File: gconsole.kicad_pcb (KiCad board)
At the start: 2 copper layers, 2 parts, among them SW1 SW_Push, U1 XIAO-ESP32-C3-DIP

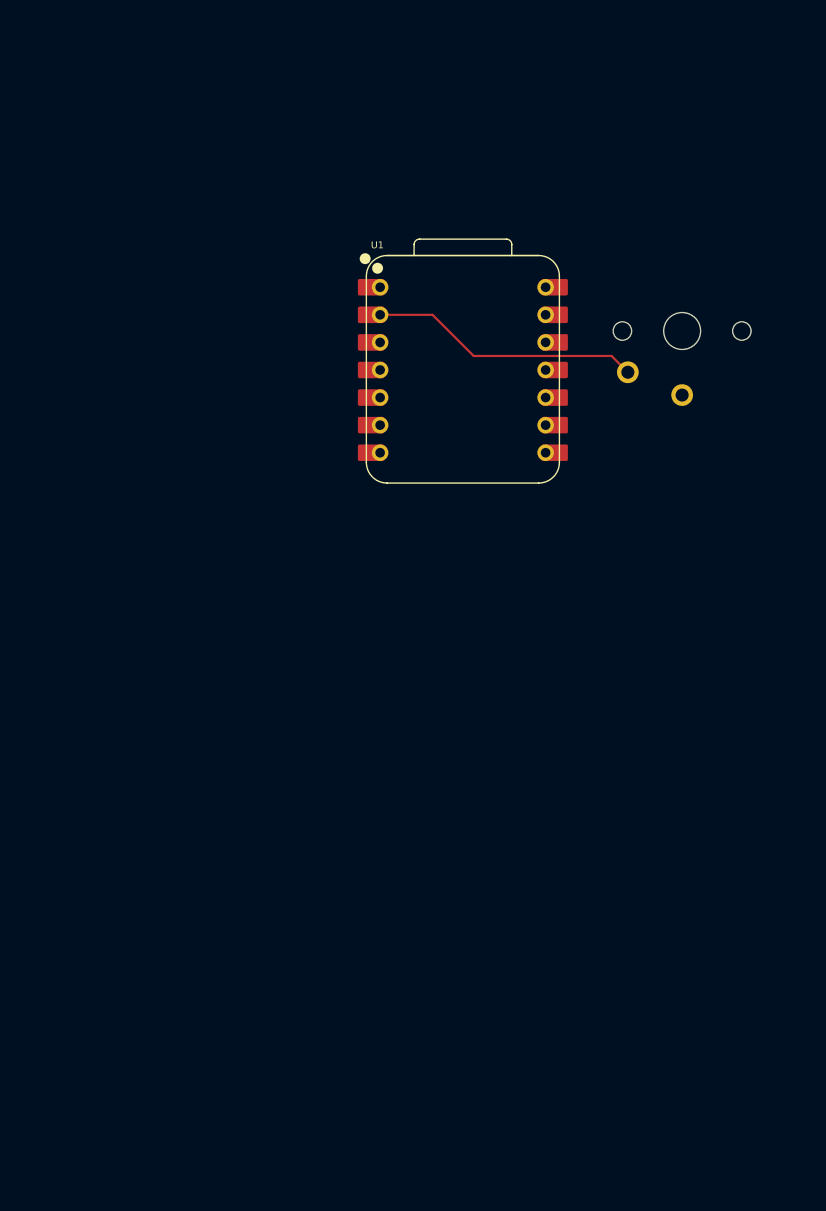
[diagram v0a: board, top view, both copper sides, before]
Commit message: Imported modules in KiCad
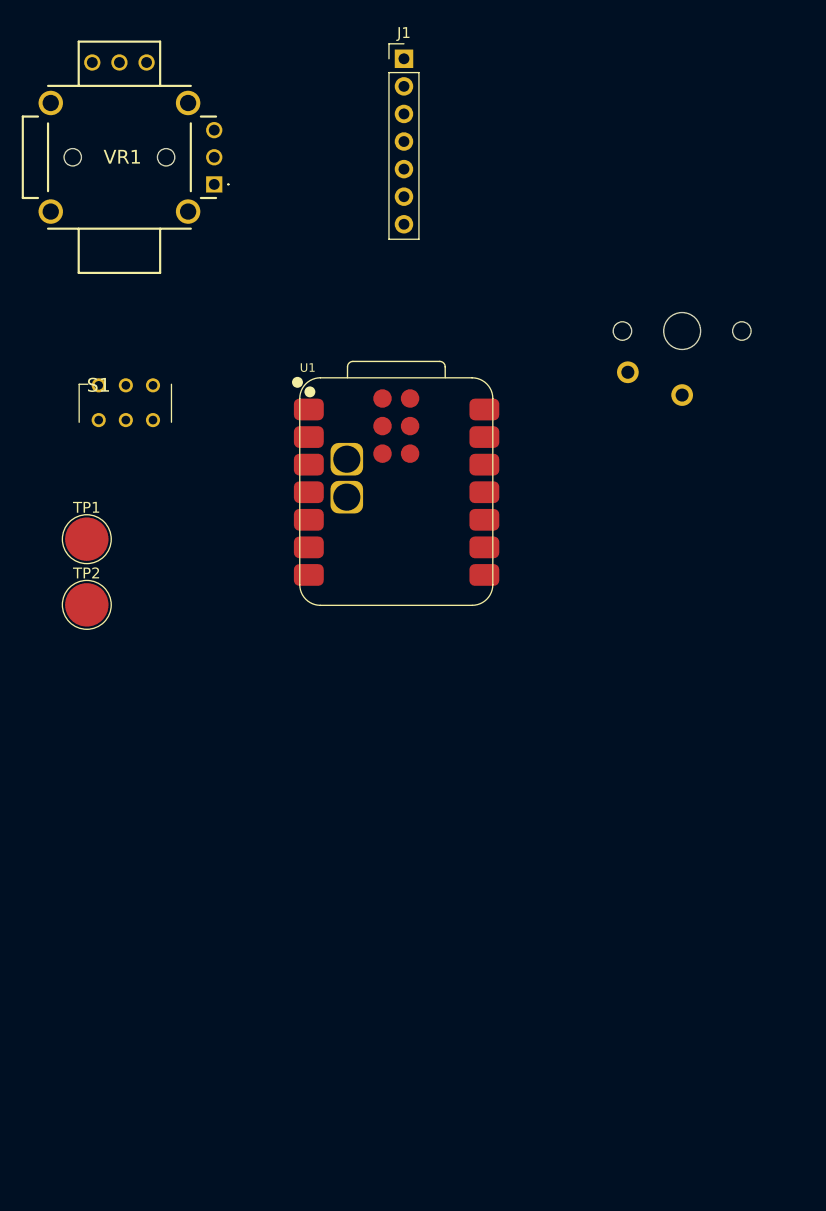
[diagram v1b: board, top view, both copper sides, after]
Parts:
- added J1: Conn_01x07_Socket, Connector_PinHeader_2.54mm:PinHeader_1x07_P2.54mm_Vertical, F.Cu at (119.4, 74.9)
- added S1: EG1271A, KiCad:EG1271, F.Cu at (91.3, 105.0)
- added TP1: TestPoint, TestPoint:TestPoint_Pad_D4.0mm, F.Cu at (90.2, 119.2)
- added TP2: TestPoint, TestPoint:TestPoint_Pad_D4.0mm, F.Cu at (90.2, 125.2)
- added VR1: RKJXV1224005, joystick:RKJXV1224005, F.Cu at (101.9, 86.5)
- U1: footprint Seeed Studio XIAO Series Library:XIAO-ESP32C3-DIP -> Seeed Studio XIAO Series Library:XIAO-ESP32C3-SMD
- moved U1 12.9 mm to (118.6, 114.8)
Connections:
- SW1 pad 1: Net-(U1-GPIO3/A1/D1) -> unconnected-(SW1-Pad1)
- U1 pad 2: Net-(U1-GPIO3/A1/D1) -> unconnected-(U1-GPIO3/A1/D1-Pad2)
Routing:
- net Net-(U1-GPIO3/A1/D1): track 25.0 -> 0.00 mm

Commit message: Finished designing PCB
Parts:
- added H1: MountingHole, MountingHole:MountingHole_3.2mm_M3, F.Cu at (145.5, 93.0)
- added H2: MountingHole, MountingHole:MountingHole_3.2mm_M3, F.Cu at (106.1, 92.9)
- added H3: MountingHole, MountingHole:MountingHole_3.2mm_M3, F.Cu at (106.2, 170.4)
- added H4: MountingHole, MountingHole:MountingHole_3.2mm_M3, F.Cu at (145.5, 170.4)
- S1, TP1, TP2: moved to B.Cu
- U1: value XIAO-ESP32-C3-DIP -> XIAO-ESP32-C3-SMD; footprint Seeed Studio XIAO Series Library:XIAO-ESP32C3-SMD -> Seeed Studio XIAO Series Library:XIAO-ESP32C3-SMD-modified; moved to B.Cu
- moved VR1 73.0 mm to (123.0, 156.4)
- moved SW1 54.1 mm to (136.7, 153.4)
- moved TP1 48.8 mm to (137.7, 130.3), turned to 180 degrees
- moved TP2 48.8 mm to (137.7, 136.4), turned to 180 degrees
- moved S1 38.8 mm to (130.0, 107.0), turned to -90 degrees
- moved J1 25.4 mm to (132.8, 96.5), turned to -90 degrees
- moved U1 4.38 mm to (114.3, 114.3), turned to -90 degrees
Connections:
- J1 pad 1: unconnected-(J1-Pin_1-Pad1) -> Net-(J1-Pin_1)
- J1 pad 2: unconnected-(J1-Pin_2-Pad2) -> Net-(J1-Pin_2)
- J1 pad 3: unconnected-(J1-Pin_3-Pad3) -> Net-(J1-Pin_3)
- J1 pad 4: unconnected-(J1-Pin_4-Pad4) -> Net-(J1-Pin_4)
- J1 pad 5: unconnected-(J1-Pin_5-Pad5) -> Net-(J1-Pin_5)
- J1 pad 6: unconnected-(J1-Pin_6-Pad6) -> +3V3
- J1 pad 7: unconnected-(J1-Pin_7-Pad7) -> GND
- S1 pad 2: unconnected-(S1-COM_1-Pad2) -> /+BAT
- S1 pad 3: unconnected-(S1-NO_1-Pad3) -> Net-(S1-NO_1)
- SW1 pad 1: unconnected-(SW1-Pad1) -> Net-(U1-GPIO20_D7_RX)
- SW1 pad 2: unconnected-(SW1-Pad2) -> GND
- TP1 pad 1: unconnected-(TP1-Pad1) -> GND
- TP2 pad 1: unconnected-(TP2-Pad1) -> /+BAT
- U1 pad 1: unconnected-(U1-GPIO2/A0/D0-Pad1) -> Net-(U1-GPIO2_A0_D0)
- U1 pad 11: unconnected-(U1-GPIO10/D10/MOSI-Pad11) -> Net-(J1-Pin_4)
- U1 pad 12: unconnected-(U1-VCC_3V3-Pad12) -> +3V3
- U1 pad 13: unconnected-(U1-GND-Pad13) -> GND
- U1 pad 15: (no net) -> Net-(S1-NO_1)
- U1 pad 16: (no net) -> GND
- U1 pad 17: (no net) -> unconnected-(U1-MTDI-Pad17)
- U1 pad 18: (no net) -> unconnected-(U1-MTDO-Pad18)
- U1 pad 19: (no net) -> unconnected-(U1-CHIP_EN-Pad19)
- U1 pad 2: unconnected-(U1-GPIO3/A1/D1-Pad2) -> Net-(U1-GPIO3_A1_D1)
- U1 pad 20: (no net) -> GND
- U1 pad 21: (no net) -> unconnected-(U1-MTMS-Pad21)
- U1 pad 22: (no net) -> unconnected-(U1-MTCK-Pad22)
- U1 pad 5: unconnected-(U1-GPIO6/D4/SDA-Pad5) -> Net-(J1-Pin_3)
- U1 pad 6: unconnected-(U1-GPIO7/D5/SCL-Pad6) -> Net-(J1-Pin_2)
- U1 pad 7: unconnected-(U1-GPIO21/D6/TX-Pad7) -> Net-(J1-Pin_1)
- U1 pad 8: unconnected-(U1-GPIO20/D7/RX-Pad8) -> Net-(U1-GPIO20_D7_RX)
- U1 pad 9: unconnected-(U1-GPIO8/D8/SCK-Pad9) -> Net-(J1-Pin_5)
- VR1 pad A1: unconnected-(VR1-CCW_1-PadA1) -> GND
- VR1 pad A2: unconnected-(VR1-WIPER_1-PadA2) -> Net-(U1-GPIO2_A0_D0)
- VR1 pad A3: unconnected-(VR1-CW_1-PadA3) -> +3V3
- VR1 pad B1: unconnected-(VR1-CCW_2-PadB1) -> GND
- VR1 pad B2: unconnected-(VR1-WIPER_2-PadB2) -> Net-(U1-GPIO3_A1_D1)
- VR1 pad B3: unconnected-(VR1-CW_2-PadB3) -> +3V3
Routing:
- net +3V3: track 0.00 -> 74.3 mm
- net Net-(U1-GPIO2_A0_D0): track 0.00 -> 56.3 mm, vias 0 -> 2
- net Net-(J1-Pin_1): track 0.00 -> 51.8 mm, vias 0 -> 2
- net Net-(U1-GPIO3_A1_D1): track 0.00 -> 46.3 mm, vias 0 -> 1
- net Net-(J1-Pin_2): track 0.00 -> 44.1 mm, vias 0 -> 2
- net Net-(J1-Pin_4): track 0.00 -> 39.8 mm, vias 0 -> 1
- net Net-(U1-GPIO20_D7_RX): track 0.00 -> 39.4 mm
- net Net-(J1-Pin_3): track 0.00 -> 31.7 mm
- net /+BAT: track 0.00 -> 30.3 mm
- net Net-(J1-Pin_5): track 0.00 -> 28.4 mm, vias 0 -> 1
- net Net-(S1-NO_1): track 0.00 -> 17.6 mm, vias 0 -> 1
- net GND: track 0.00 -> 7.26 mm
- added copper zone on B.Cu, net GND
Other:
- board outline added: 46 x 84.1 mm
